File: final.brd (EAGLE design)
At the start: 76 x 60.4 mm, 84 parts, among them IC1 LD117ADT12TR, IC2 MEGA8-AI, Q2 32.768kHz, U2 DS1307

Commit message: fixed big issue on driver
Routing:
- net SEGMENT-E: track 89.7 -> 86.5 mm
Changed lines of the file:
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@@
 <wire x1="21.5138" y1="54.151128125" x2="22.861671875" y2="55.499" width="0.2" layer="16"/>
 <via x="22.861671875" y="55.499" extent="1-16" drill="0.35"/>
-<wire x1="38.0746" y1="55.499" x2="34.823" y2="55.499" width="0.2" layer="16"/>
 <wire x1="15.4212125" y1="53.9242" x2="15.45238125" y2="53.89303125" width="0.2" layer="1"/>
 <contactref element="T18" pad="C"/>

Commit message: small details done
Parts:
- moved T28 0.36 mm to (53.4, 53.2)
- moved U$7 0.18 mm to (43.6, 7.11)
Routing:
- net N$11: track 45.5 -> 52.7 mm
- net GND: track 455.2 -> 457.2 mm, vias 13 -> 14
- net 20VD: track 113.9 -> 112.0 mm
- net VCC: track 59.1 -> 58.0 mm
- net N$93: track 19.4 -> 20.2 mm
- net N$12: track 37.1 -> 37.8 mm
- net N$37: track 49.7 -> 49.2 mm
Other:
- outline, holes or cut-outs redrawn

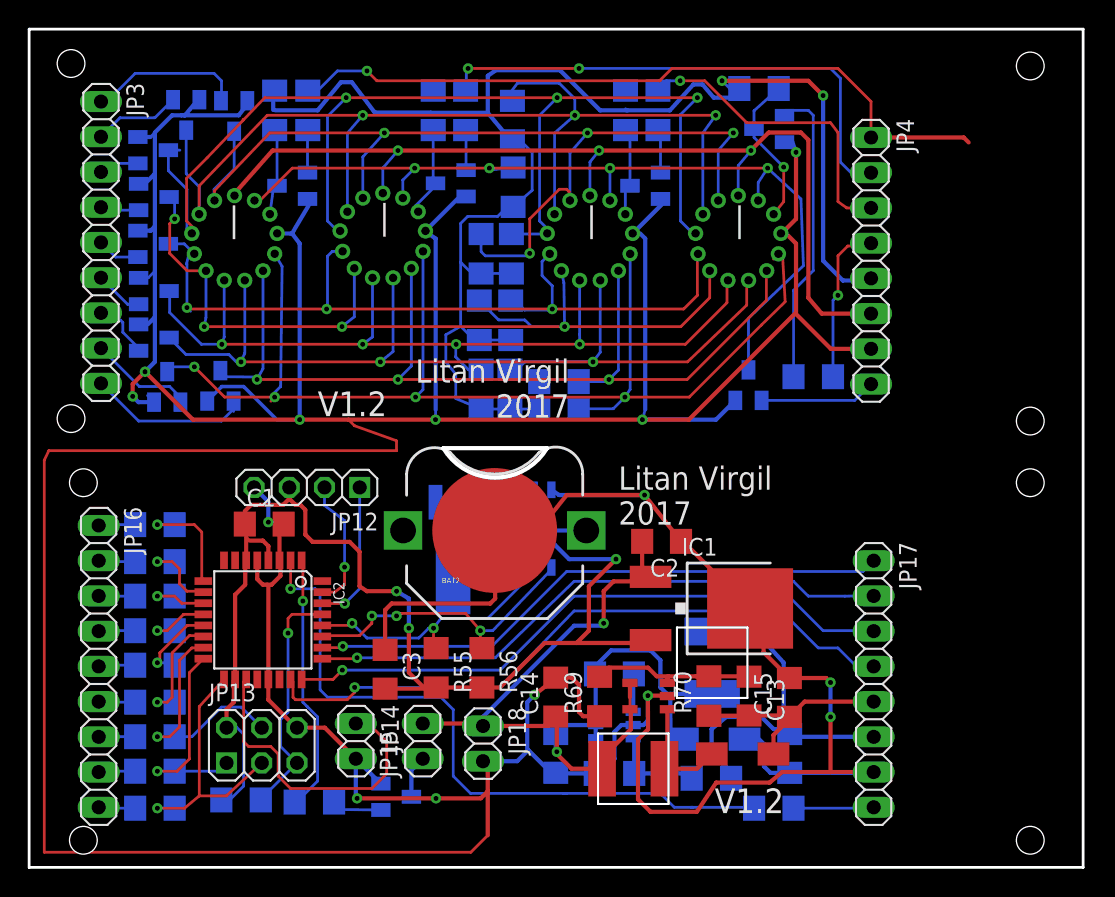
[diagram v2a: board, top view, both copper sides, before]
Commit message: thicker traces for switching supplies. milling almost done
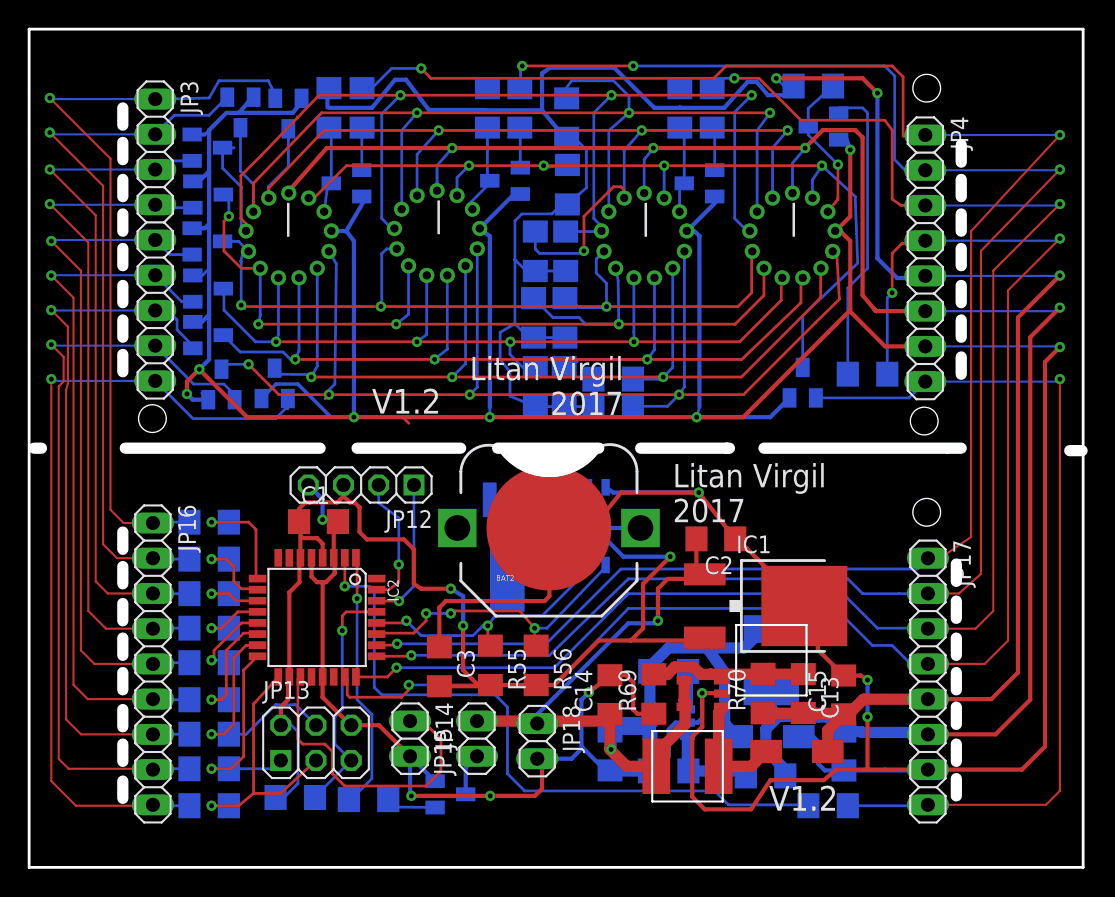
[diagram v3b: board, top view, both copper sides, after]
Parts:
- moved U$8 4.27 mm to (53.5, 14.9), turned to 90 degrees
- moved JP17 3.92 mm to (64.8, 13.4)
- moved T15 3.92 mm to (18.7, 54.4)
- moved T23 3.92 mm to (17.7, 34.9)
- moved BAT2 3.92 mm to (37.5, 24.5)
- moved C1 3.92 mm to (20.9, 24.9)
- moved C13 3.92 mm to (55.8, 12.5)
- moved C14 3.92 mm to (41.9, 12.5)
- moved C15 3.92 mm to (58.7, 12.4)
- moved C16 3.92 mm to (41.9, 8.40)
- moved C17 3.92 mm to (46.1, 14.1)
- moved C18 3.92 mm to (58.8, 8.39)
- moved C2 3.92 mm to (49.5, 23.7)
- moved C3 3.92 mm to (29.6, 14.5)
- moved IC1 3.92 mm to (53.5, 18.8)
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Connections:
- removed net 1.5VD: JP4.6, U$1.1, U$2.1, U$3.1, U$4.1
- removed net N$11: JP4.1, R16.2
- removed net N$12: JP4.2, R8.2
- removed net N$13: JP4.3, R9.2
- removed net N$16: JP4.4, R10.2
- removed net N$2: JP3.2, T17.B
- removed net N$20: JP3.7, T24.B
- removed net N$23: JP3.6, T19.B
- removed net N$26: JP3.1, T15.B
- removed net N$27: JP16.3, R26.1
- removed net N$28: JP3.3, T18.B
- removed net N$29: JP3.4, T16.B
- removed net N$3: JP16.9, R35.1
- removed net N$30: JP16.2, R25.1
- removed net N$33: JP3.8, T20.B
- removed net N$34: JP3.9, T23.B
- removed net N$38: JP4.8, T22.B
- removed net N$4: JP16.8, R34.1
- removed net N$41: JP17.8, R14.2
- removed net N$48: JP16.1, R24.1
- removed net N$5: JP3.5, T21.B
- removed net N$6: JP16.7, R32.1
- removed net N$7: JP16.6, R33.1
- removed net N$8: JP16.5, R30.1
- removed net N$9: JP16.4, R28.1
- new net SEG1: JP17.8, JP4.8, R14.2, T22.B
- new net SEG10: JP16.9, JP3.9, R35.1, T23.B
- new net SEG2: JP16.1, JP3.1, R24.1, T15.B
- new net SEG3: JP16.2, JP3.2, R25.1, T17.B
- new net SEG4: JP16.3, JP3.3, R26.1, T18.B
- new net SEG5: JP16.4, JP3.4, R28.1, T16.B
- new net SEG6: JP16.5, JP3.5, R30.1, T21.B
- new net SEG7: JP16.6, JP3.6, R33.1, T19.B
- new net SEG8: JP16.7, JP3.7, R32.1, T24.B
- new net SEG9: JP16.8, JP3.8, R34.1, T20.B
- net 1V5: now also JP4.6, U$1.1, U$2.1, U$3.1, U$4.1
- net 20V: now also JP4.5, R31.2
- net 20VD: no longer JP4.5, R31.2
- net SELECT1: now also JP4.1, R16.2
- net SELECT2: now also JP4.3, R9.2
- net SELECT3: now also JP4.2, R8.2
- net SELECT4: now also JP4.4, R10.2
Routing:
- net 1V5: track 27.6 -> 139.3 mm, vias 0 -> 4
- net SELECT1: track 42.5 -> 133.8 mm, vias 1 -> 3
- net 20V: track 17.0 -> 101.4 mm, vias 0 -> 3
- net SELECT3: track 43.8 -> 127.1 mm, vias 1 -> 4
- net 1.5VD: track 70.5 -> 0.00 mm, vias 3 -> 0
- net SELECT2: track 46.1 -> 115.1 mm, vias 1 -> 3
- net SEG1: track 0.00 -> 63.6 mm, vias 0 -> 1
- net SEG10: track 0.00 -> 61.9 mm, vias 0 -> 1
- net SELECT4: track 47.9 -> 106.3 mm, vias 1 -> 3
- net SEG9: track 0.00 -> 57.7 mm, vias 0 -> 1
- net SEG2: track 0.00 -> 57.5 mm, vias 0 -> 1
- net SEG3: track 0.00 -> 54.0 mm, vias 0 -> 1
- net SEG8: track 0.00 -> 53.4 mm, vias 0 -> 1
- net N$11: track 52.7 -> 0.00 mm, vias 1 -> 0
- net SEG7: track 0.00 -> 52.1 mm, vias 0 -> 1
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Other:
- outline, holes or cut-outs redrawn

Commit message: added pin naming
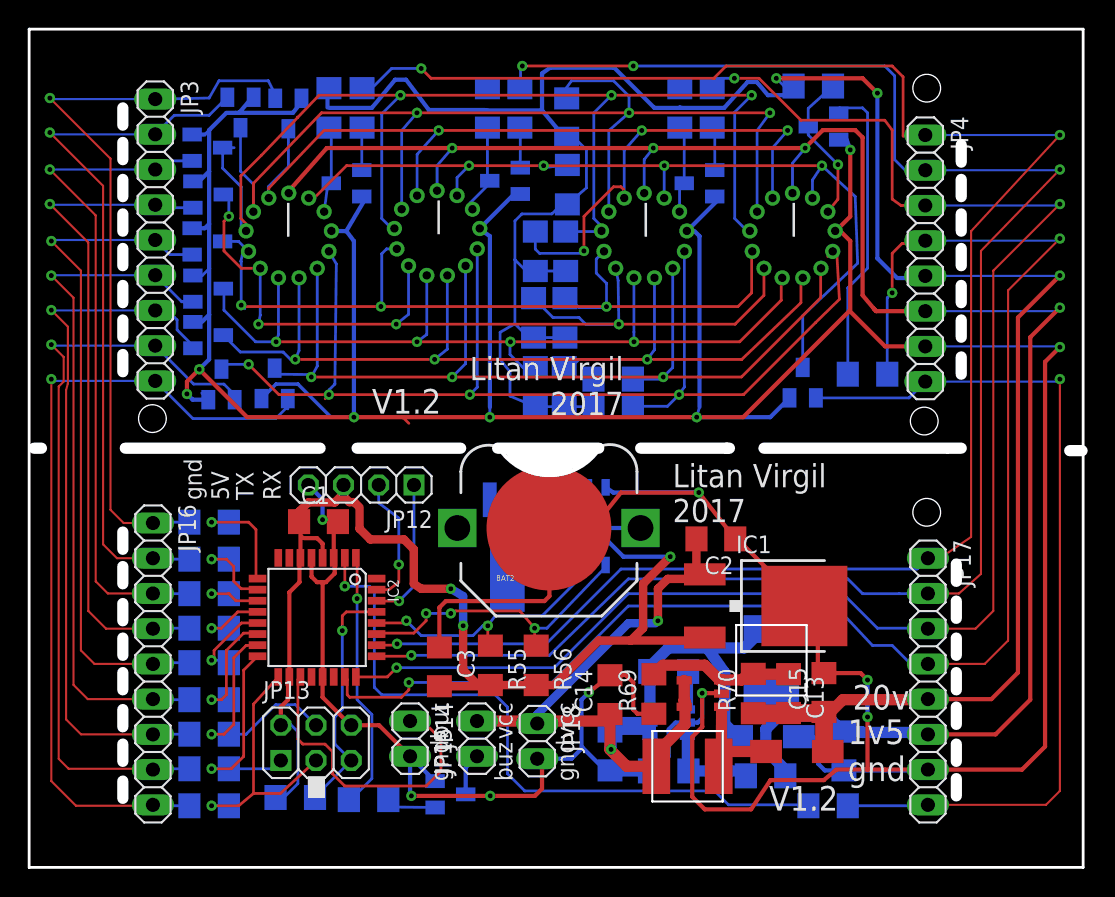
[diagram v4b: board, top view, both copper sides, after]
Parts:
- moved C15 1.43 mm to (57.3, 12.6)
- moved C13 1.07 mm to (54.8, 12.5)
- moved R70 0.71 mm to (52.2, 12.5)
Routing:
- net 20V: track 101.4 -> 89.4 mm
- net N$91: track 17.9 -> 12.3 mm
- net +5V: track 92.8 -> 97.1 mm
- net GND: track 411.6 -> 412.3 mm
- net N$90: track 12.0 -> 12.6 mm
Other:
- board text added: "1v5"
- board text added: "20v"
- board text added: "5V"
- board text added: "RX"
- board text added: "TX"
- board text added: "but"
- board text added: "buz"
- board text added: "gnd"
- board text added: "vcc"

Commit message: fixed mirrored vfd layout
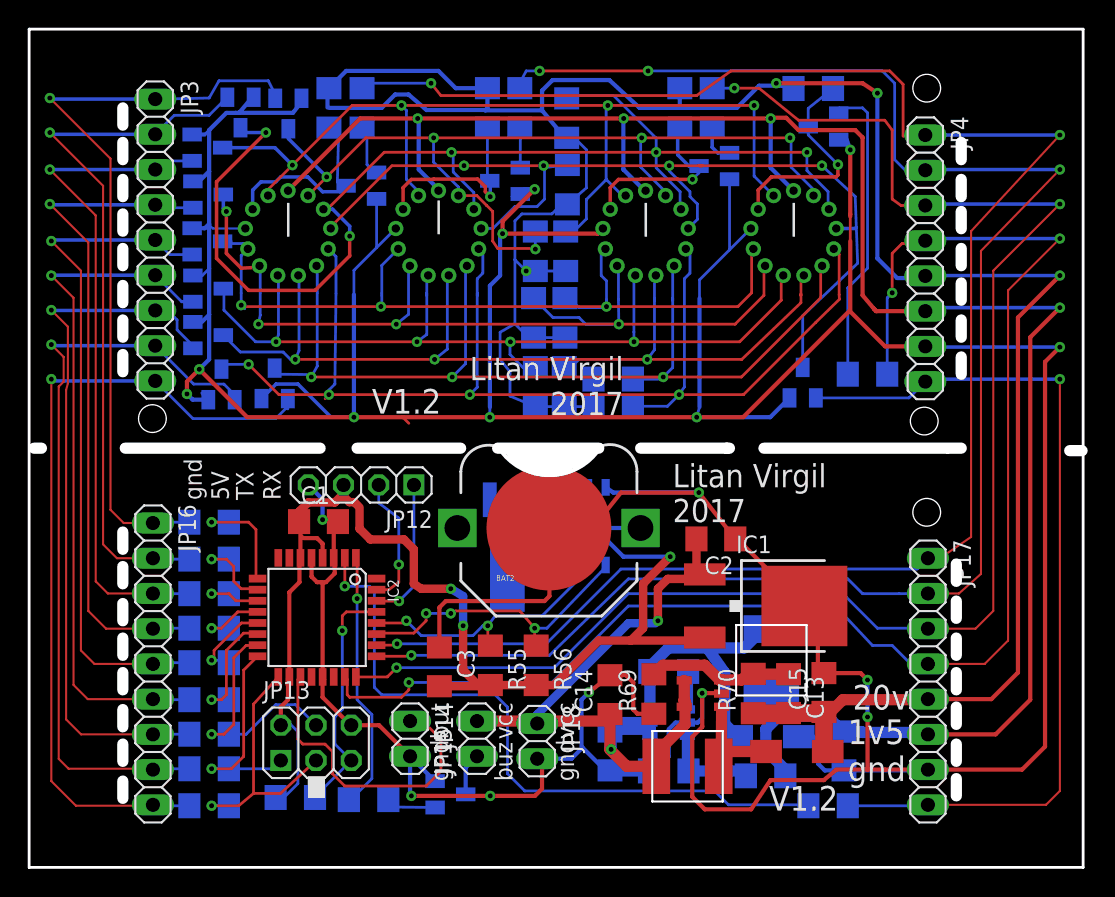
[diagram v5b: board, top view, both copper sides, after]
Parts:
- R71: value 10k -> 100k
- R72: value 10k -> 62k
- U$1, U$2, U$3, U$4: value VFD -> (none)
- moved T27 1.64 mm to (49.4, 50.6)
- moved T25 1.08 mm to (24.0, 49.1)
- moved U$3 0.20 mm to (44.5, 45.7)
- moved U$4 0.19 mm to (55.1, 45.7)
- moved U$1 0.18 mm to (18.7, 45.7)
- moved R31 0.18 mm to (56.5, 56.2)
- moved U$2 0.10 mm to (29.5, 45.7)
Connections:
- removed net 20VD: R1.2, R11.2, R13.2, R15.2, R17.2, R2.2, R21.2, R27.2, R3.2, R4.2, R5.2, R6.2, R7.2
- net 20V: now also R1.2, R11.2, R13.2, R15.2, R17.2, R2.2, R21.2, R27.2, R3.2, R4.2, R5.2, R6.2, R7.2
- net GND: now also U$1.11, U$2.11, U$3.11, U$4.11; no longer U$1.4, U$2.4, U$3.4, U$4.4
- net N$14: now also U$1.12; no longer U$1.3
- net N$18: now also U$2.12; no longer U$2.3
- net N$22: now also U$3.12; no longer U$3.3
- net N$24: now also U$4.12; no longer U$4.3
- net SEGMENT-A: now also R5.1, T19.C, U$1.8, U$2.8, U$3.8, U$4.8; no longer R15.1, T24.C, U$1.7, U$2.7, U$3.7, U$4.7
- net SEGMENT-B: now also R2.1, T16.C, U$1.9, U$2.9, U$3.9, U$4.9; no longer R13.1, T23.C, U$1.6, U$2.6, U$3.6, U$4.6
- net SEGMENT-C: now also R4.1, T18.C, U$1.13, U$2.13, U$3.13, U$4.13; no longer R11.1, T22.C, U$1.2, U$2.2, U$3.2, U$4.2
- net SEGMENT-D: now also U$1.3, U$2.3, U$3.3, U$4.3; no longer U$1.12, U$2.12, U$3.12, U$4.12
- net SEGMENT-DP: now also R7.1, T21.C, U$1.10, U$2.10, U$3.10, U$4.10; no longer R6.1, T20.C, U$1.5, U$2.5, U$3.5, U$4.5
- net SEGMENT-E: now also R11.1, T22.C, U$1.4, U$2.4, U$3.4, U$4.4; no longer R4.1, T18.C, U$1.11, U$2.11, U$3.11, U$4.11
- net SEGMENT-F: now also R13.1, T23.C, U$1.6, U$2.6, U$3.6, U$4.6; no longer R2.1, T16.C, U$1.9, U$2.9, U$3.9, U$4.9
- net SEGMENT-G: now also U$1.2, U$2.2, U$3.2, U$4.2; no longer U$1.13, U$2.13, U$3.13, U$4.13
- net SEGMENT-H: now also R15.1, T24.C, U$1.7, U$2.7, U$3.7, U$4.7; no longer R5.1, T19.C, U$1.8, U$2.8, U$3.8, U$4.8
- net SEGMENT-Q: now also R6.1, T20.C, U$1.5, U$2.5, U$3.5, U$4.5; no longer R7.1, T21.C, U$1.10, U$2.10, U$3.10, U$4.10
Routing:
- net 20V: track 89.4 -> 187.0 mm, vias 3 -> 4
- net 20VD: track 85.7 -> 0.00 mm
- net SEGMENT-Q: track 60.1 -> 89.3 mm, vias 3 -> 4
- net SEGMENT-DP: track 88.0 -> 60.8 mm, vias 4 -> 3
- net SEGMENT-E: track 86.5 -> 71.8 mm, vias 3 -> 4
- net GND: track 412.3 -> 425.4 mm, vias 15 -> 17
- net SEGMENT-D: track 78.5 -> 89.7 mm, vias 3 -> 5
- net SEGMENT-H: track 63.2 -> 71.9 mm, vias 4 -> 3
- net N$14: track 6.27 -> 14.2 mm
- net SEGMENT-G: track 73.3 -> 65.5 mm, vias 4 -> 5
- net N$18: track 6.77 -> 14.3 mm, vias 0 -> 1
- net SEGMENT-A: track 71.0 -> 64.1 mm, vias 3 -> 4
- net 1V5: track 139.3 -> 145.6 mm
- net N$22: track 6.78 -> 12.8 mm, vias 0 -> 1
- net SEGMENT-C: track 64.5 -> 70.2 mm
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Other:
- outline, holes or cut-outs redrawn

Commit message: added groundplane, replaced 5v regulator, added extra capacitors and optional diode / 0kresistor
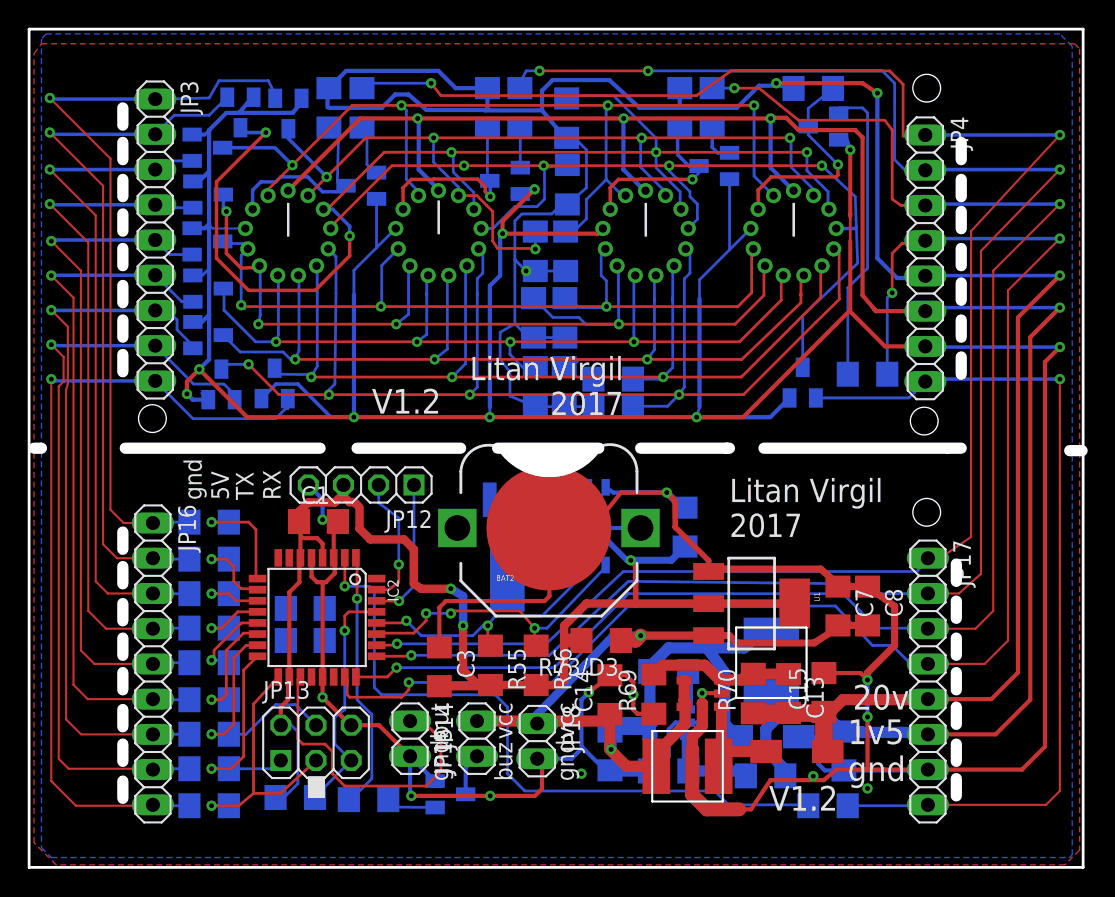
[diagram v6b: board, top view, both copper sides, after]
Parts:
- removed C2: 22uF, eagle-ltspice:C1206
- removed IC1: LD117ADT12TR, v-reg:DPACK
- added C4, C5, C6: 10uF, eagle-ltspice:C1206
- added C7, C8: 22uF, eagle-ltspice:C1206
- added R73/D3: 0k, eagle-ltspice:R1206
- added U1: NCP1117ST50T3G, NCP1117ST50T3G:SOT223
- moved U$8 0.18 mm to (53.5, 14.8)
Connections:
- net +5V: now also C4.2, C5.2, C6.2, R73/D3.2, U1.2, U1.4; no longer IC1.3
- net GND: now also C4.1, C5.1, C6.1, C7.1, C8.1, U1.1; no longer C2.1, IC1.4
- net VCC: now also C7.2, C8.2, R73/D3.1, U1.3; no longer C2.2, IC1.1
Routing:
- net +5V: track 97.1 -> 106.7 mm
- net VCC: track 79.2 -> 87.5 mm
- net GND: track 425.4 -> 432.3 mm, vias 17 -> 19
- net N$93: track 25.2 -> 24.6 mm
- added copper zone on layer 1, net GND
- added copper zone on layer 16, net GND
